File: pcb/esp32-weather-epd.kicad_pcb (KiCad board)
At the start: 2 copper layers, 67 parts, among them J1 S2B-PH-K-S(LF)(SN), Q1 S8050, Q2 S8050, Q3 BRCS150P02ZJ, Q4 SI1308EDL-T1-GE3, U1 CH340X, U2 TP4056X, U3 RT9080-33GJ5, U4 ESP32-WROOM-32E, U5 BME680

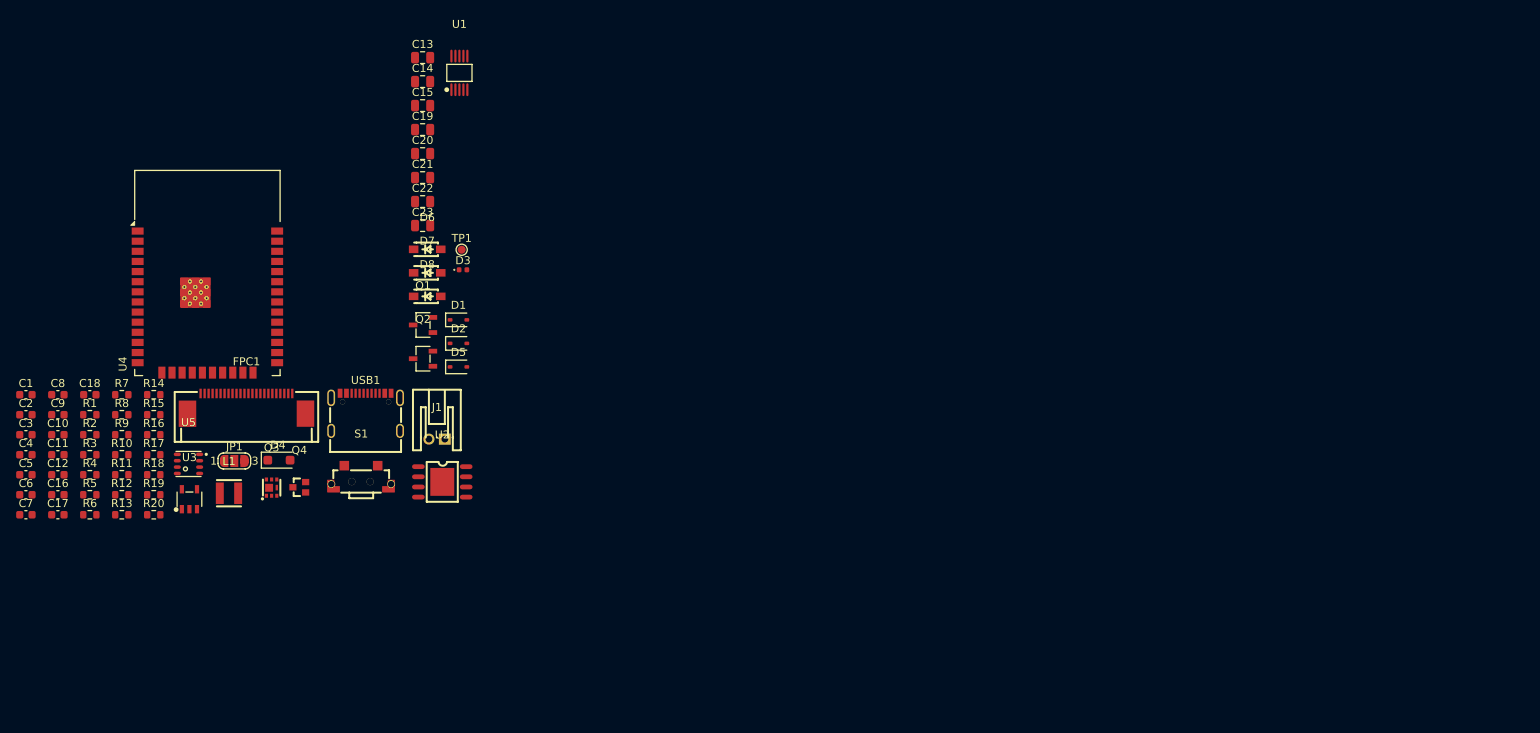
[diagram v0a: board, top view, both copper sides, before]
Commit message: rework schematic and first draft component placement
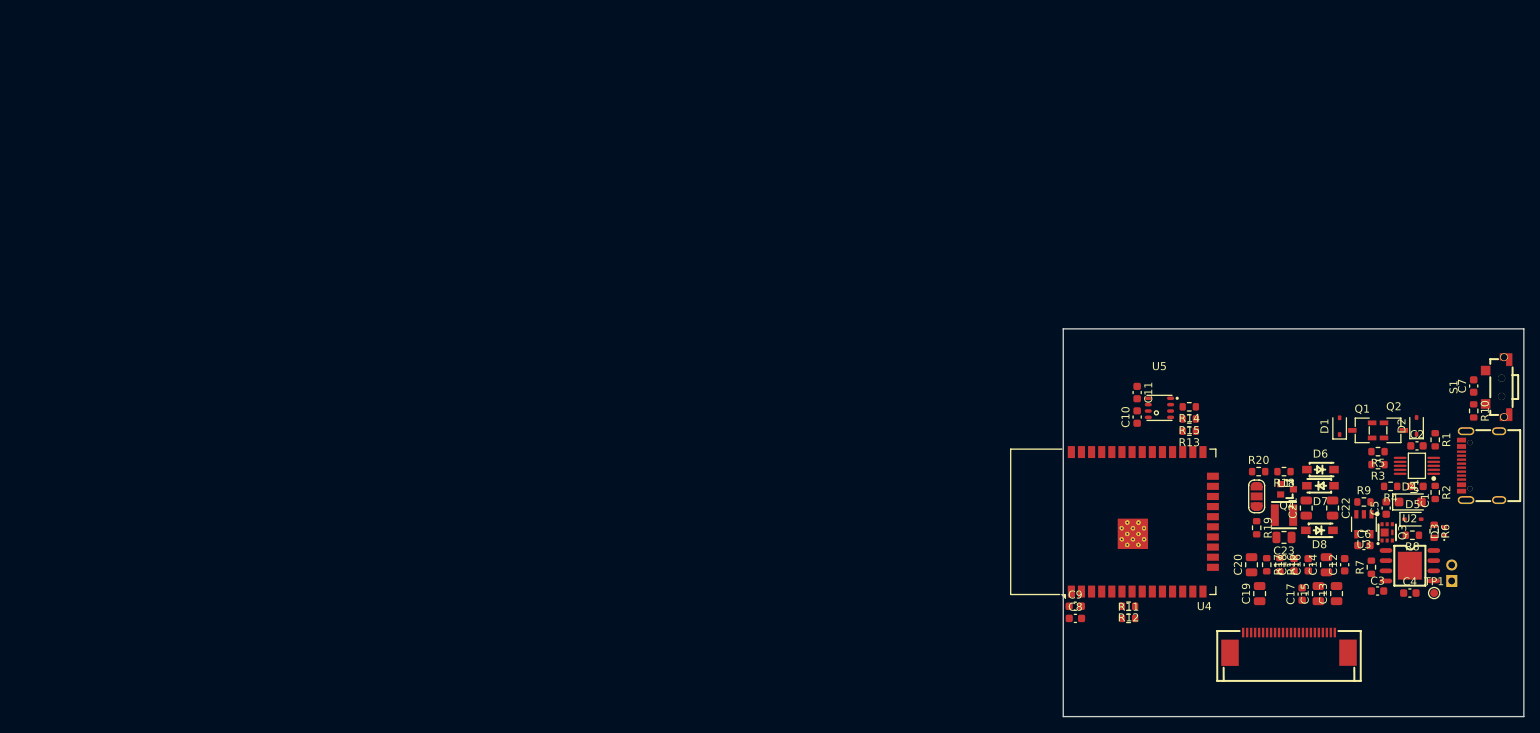
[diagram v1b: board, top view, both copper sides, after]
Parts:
- J1: moved to B.Cu
- moved C7 182.3 mm to (226.5, 86.2), turned to 90 degrees
- moved C1 174.9 mm to (219.4, 98.8)
- moved C2 174.6 mm to (219.4, 93.7)
- moved C4 174.5 mm to (218.5, 112.1)
- moved C5 170.7 mm to (215.5, 101.5), turned to 90 degrees
- moved C3 170.7 mm to (214.4, 111.9)
- moved R10 169.7 mm to (226.5, 89.3), turned to -90 degrees
- moved R2 168.9 mm to (221.7, 99.5), turned to -90 degrees
- moved R1 168.8 mm to (221.7, 92.9), turned to -90 degrees
- moved R6 168.7 mm to (221.5, 104.4), turned to -90 degrees
- moved C6 168.0 mm to (212.7, 106.2)
- moved R4 163.2 mm to (216.1, 98.8), turned to 180 degrees
- moved R8 162.6 mm to (218.8, 104.9), turned to 180 degrees
- moved C12 161.8 mm to (210.3, 108.6), turned to 90 degrees
- moved R5 161.7 mm to (214.5, 94.4), turned to 180 degrees
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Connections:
- U4 pad 25: unconnected-(U4-IO0-Pad25) -> /IO-0/D5
- U4 pad 34: unconnected-(U4-RXD0/IO3-Pad34) -> /D0(RX)
- U4 pad 35: unconnected-(U4-TXD0/IO1-Pad35) -> /D1(TX)
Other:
- board outline added: 57.8 x 48.6 mm
